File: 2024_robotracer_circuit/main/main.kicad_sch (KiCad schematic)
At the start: 18 parts, among them J1 Conn_01x06, J2 Conn_02x05_Odd_Even, J3 Conn_02x05_Odd_Even, SW1 SW_Push, U1 STM32F405RGTx

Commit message: 進めた
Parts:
- added C11, C14, C15, C18, C20, C21, C23: 0.1u, symbol Device:C_Small
- added C12, C13: 220u, symbol Device:C_Polarized_Small
- added C16, C17, C19, C22: 100u, symbol Device:C_Polarized_Small
- added J4, J5, J6: Conn_01x02, symbol Connector_Generic:Conn_01x02
- added R2: R, symbol Device:R
- added SW2: SW_DPDT_x2, symbol Switch:SW_DPDT_x2
- added U3, U4: ~, symbol mylib:AM2837
- added U5: ~, symbol mylib:BP5293-33
- added U6: ~, symbol mylib:BP5293-50
- added U7: ~, symbol mylib:SSM6J808R
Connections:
- net +3.3V: now also C17.1, C18.1, U5.3 (VOUT)
- net +5V: now also C21.1, C22.1, U6.3 (VOUT)
- net GND: now also C11.2, C12.2, C13.2, C14.2, C15.2, C16.2, C17.2, C18.2, C19.2, C20.2, C21.2, C22.2, C23.2, J6.2 (Pin_2), SW2.2 (B), U3.3 (GND), U4.3 (GND), U5.2 (GND), U6.2 (GND)
- new net: J6.1 (Pin_1), R2.1, U7.4 (SOURCE)
- new net: J4.1 (Pin_1), U3.7 (OUT_A), U3.8 (OUT_A)
- new net: J4.2 (Pin_2), U3.5 (OUT_B), U3.6 (OUT_B)
- new net: R2.2, SW2.1 (A), U7.3 (GATE)
- new net: J5.2 (Pin_2), U4.5 (OUT_B), U4.6 (OUT_B)
- new net: J5.1 (Pin_1), U4.7 (OUT_A), U4.8 (OUT_A)
- new net +BATT: C11.1, C12.1, C13.1, C14.1, C15.1, C16.1, C19.1, C20.1, C23.1, U3.4 (VCC), U4.4 (VCC), U5.1 (VIN), U6.1 (VIN), U7.1 (DRAIN_1), U7.2 (DRAIN_2), U7.5 (DRAIN_3), U7.6 (DRAIN_4)
- new net MOTOR1_IN_A: U3.1 (IN_A), U4.1 (IN_A)
- new net MOTOR1_IN_B: U3.2 (IN_B), U4.2 (IN_B)
- no-connect marks 14 -> 15
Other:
- moved on the sheet: C1, C10, C2, C3, C4, C5, C6, C7, C8, C9, FB1, J1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

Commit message: 途中
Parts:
- added BZ1: Buzzer, symbol Device:Buzzer
- added C24: 220u, symbol Device:C_Polarized_Small
- added C25: 0.1u, symbol Device:C_Small
- added C26, C27: 100u, symbol Device:C_Polarized_Small
- added D1: D, symbol Device:D
- added D2, D3, D4: LED_Small, symbol Device:LED_Small
- added J10, J11: Conn_01x03, symbol Connector_Generic:Conn_01x03
- added J7: Micro_SD_Card_Det1, symbol Connector:Micro_SD_Card_Det1
- added J8: Conn_01x04, symbol Connector_Generic:Conn_01x04
- added J9: Conn_01x06, symbol Connector_Generic:Conn_01x06
- added R11, R12, R13, R14, R15, R16, R17: 22k, symbol Device:R_Small
- added R18, R19, R20, R21, R22, R25, R28: 47k, symbol Device:R_Small
- added R23, R24, R31, R32, R33: R_Small, symbol Device:R_Small
- added R26, R29, R3, R5, R7, R9: 4.7, symbol Device:R_Small
- added R34, R35, R36, R37, R38, R39, R4, R6: 1k, symbol Device:R_Small
- added U10, U12, U14, U17, U18, U20, U9: ~, symbol mylib:MTN2306AN3
- added U11, U13, U15, U19, U21, U8: ~, symbol mylib:LBR-127HLD
- added U16: ~, symbol mylib:AE-BMX055
- J4, J5: value Conn_01x02 -> PA_2p
- J6: value Conn_01x02 -> XT_2p
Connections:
- net +3.3V: now also C24.1, C25.1, J7.4 (VDD), J8.1 (Pin_1), R11.1, R12.1, R13.1, R14.1, R15.1, R16.1, R32.1, R34.1, R35.1, U16.4 (3V3)
- net +5V: now also J10.1 (Pin_1), J11.1 (Pin_1), J9.1 (Pin_1), R33.1, R36.1, R37.1, R38.1, R39.1, R4.1, R6.1, U11.1 (anode), U13.1 (anode), U15.1 (anode), U19.1 (anode), U21.1 (anode), U8.1 (anode)
- net +BATT: now also BZ1.1 (+), C26.1, C27.1, D1.1 (K), R23.1, R31.1
- net GND: now also C24.2, C25.2, C26.2, C27.2, D2.1 (K), D3.1 (K), D4.1 (K), J10.3 (Pin_3), J11.3 (Pin_3), J7.10 (SHIELD), J7.6 (VSS), J8.4 (Pin_4), J9.6 (Pin_6), R17.2, R18.2, R19.2, R20.2, R21.2, R22.2, R24.2, R25.2, R28.2, U10.3 (S), U11.3 (E), U12.3 (S), U13.3 (E), U14.3 (S), U15.3 (E), U16.1 (GND), U17.3 (S), U18.3 (S), U19.3 (E), U20.3 (S), U21.3 (E), U8.3 (E), U9.3 (S)
- new net: R29.1, U21.2 (cathode)
- new net: R29.2, U20.2 (D)
- new net: R26.1, U19.2 (cathode)
- new net: R26.2, U18.2 (D)
- new net: R3.2, U9.2 (D)
- new net: R5.1, U11.2 (cathode)
- new net: D3.2 (A), R32.2
- new net: R3.1, U8.2 (cathode)
- new net: J7.1 (DAT2), R16.2
- new net: R9.1, U15.2 (cathode)
- new net: R9.2, U14.2 (D)
- new net: D4.2 (A), R33.2
- new net: R5.2, U10.2 (D)
- new net: J7.8 (DAT1), R12.2
- new net: D2.2 (A), R31.2
- new net: BZ1.2 (-), D1.2 (A), U17.2 (D)
- new net: J7.2 (DAT3/CD), R15.2
- new net: R7.1, U13.2 (cathode)
- new net: R7.2, U12.2 (D)
- new net BATT_REF: R23.2, R24.1
- new net BZ_PWM: R22.1, U17.1 (G)
- new net IMU_SCL: U16.3 (SCL)
- new net IMU_SDA: U16.2 (SDA)
- new net LCD_SCL: J8.3 (Pin_3), R35.2
- new net LCD_SDA: J8.2 (Pin_2), R34.2
- new net SDIO_CK: J7.5 (CLK), R17.1
- new net SDIO_CMD: J7.3 (CMD), R14.2
- new net SDIO_D0: J7.7 (DAT0), R13.2
- new net SDIO_SW: J7.9 (DET), R11.2
- new net SENSOR0_ADC: J9.2 (Pin_2), R36.2, U8.4 (C)
- new net SENSOR0_PWM: R18.1, U9.1 (G)
- new net SENSOR1_ADC: J9.3 (Pin_3), R37.2, U11.4 (C)
- new net SENSOR1_PWM: R19.1, U10.1 (G)
- new net SENSOR2_ADC: J9.4 (Pin_4), R38.2, U13.4 (C)
- new net SENSOR2_PWM: R20.1, U12.1 (G)
- new net SENSOR3_ADC: J9.5 (Pin_5), R39.2, U15.4 (C)
- new net SENSOR3_PWM: R21.1, U14.1 (G)
- new net SENSOR_L_ADC: J10.2 (Pin_2), R4.2, U19.4 (C)
- new net SENSOR_L_PWM: R25.1, U18.1 (G)
- new net SENSOR_R_ADC: J11.2 (Pin_2), R6.2, U21.4 (C)
- new net SENSOR_R_PWM: R28.1, U20.1 (G)
- no-connect marks 15 -> 17
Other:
- moved on the sheet: C1, C10, C11, C12, C13, C14, C15, C16, C17, C18, C19, C2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

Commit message: ピン割り当て
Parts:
- R1: value R -> 10k
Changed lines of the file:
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@@
 			)
 		)
-		(property "Value" "R"
+		(property "Value" "10k"
 			(at 308.61 74.9299 0)
 			(effects

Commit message: デザインルールOK
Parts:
- added D10, D11, D12, D13, D14, D15, D5, D6, D7, D8, D9: LED_Small, symbol Device:LED_Small
- added FB2: FerriteBead_Small, symbol Device:FerriteBead_Small
- added J12: Conn_01x04, symbol Connector_Generic:Conn_01x04
- added J14: Conn_01x06, symbol Connector_Generic:Conn_01x06
- added R10, R27, R30, R40, R41, R42, R43, R44, R45, R46, R8: R_Small, symbol Device:R_Small
- added U22: ~, symbol mylib:SKRHAAE010
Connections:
- net BATT_REF is gone; now on net BATT_REF_ADC: R23.2, R24.1
- net SWCLC is gone; now on net SWCLK: J1.2 (Pin_2)
- net +3.3V: now also J12.1 (Pin_1), J14.1 (Pin_1)
- net BZ_PWM: now also U1.35 (PB14)
- net ENC1_A: now also U1.58 (PB6)
- net ENC1_B: now also U1.59 (PB7)
- net ENC2_A: now also U1.37 (PC6)
- net ENC2_B: now also U1.38 (PC7)
- net GND: now also D10.1 (K), D11.1 (K), D12.1 (K), D13.1 (K), D14.1 (K), D15.1 (K), D5.1 (K), D6.1 (K), D7.1 (K), D8.1 (K), D9.1 (K), FB2.1, J12.4 (Pin_4), J14.6 (Pin_6), U22.5 (Common)
- net GNDA: now also FB2.2
- net IMU_SCL: now also U1.61 (PB8)
- net IMU_SDA: now also U1.62 (PB9)
- net LCD_SCL: now also U1.29 (PB10)
- net LCD_SDA: now also U1.30 (PB11)
- net MOTOR1_IN_A: now also U1.41 (PA8); no longer U4.1 (IN_A)
- net MOTOR1_IN_B: now also U1.42 (PA9); no longer U4.2 (IN_B)
- net SDIO_CK: now also U1.53 (PC12)
- net SDIO_CMD: now also U1.54 (PD2)
- net SDIO_D0: now also U1.39 (PC8)
- net SDIO_SW: now also U1.50 (PA15)
- net SENSOR0_ADC: now also U1.14 (PA0)
- net SENSOR1_ADC: now also U1.15 (PA1)
- net SENSOR2_ADC: now also U1.16 (PA2)
- net SENSOR3_ADC: now also U1.17 (PA3)
- net SENSOR_L_ADC: now also U1.20 (PA4)
- net SENSOR_R_ADC: now also U1.21 (PA5)
- net SWDIO: now also U1.46 (PA13)
- net SWO: now also U1.55 (PB3)
- net SPI_MISO_GP: now reaches U1.10 (PC2)
- net SPI_MISO_GP: now also J14.2 (Pin_2)
- net SPI_MOSI_GP: now reaches U1.11 (PC3)
- net SPI_MOSI_GP: now also J14.3 (Pin_3)
- net LED3: now reaches U1.2 (PC13)
- net LED3: now also R30.1
- net BATT_REF_ADC: now reaches U1.22 (PA6)
- net SW_A: now reaches U1.23 (PA7)
- net SW_A: now also U22.1 (A)
- net SW_B: now reaches U1.24 (PC4)
- net SW_B: now also U22.4 (B)
- net SW_Center: now reaches U1.25 (PC5)
- net SW_Center: now also U22.2 (Center)
- net SW_C: now reaches U1.26 (PB0)
- net SW_C: now also U22.3 (C)
- net SW_D: now reaches U1.27 (PB1)
- net SW_D: now also U22.6 (D)
- net LED9: now reaches U1.28 (PB2)
- net LED9: now also R45.1
- net LED4: now reaches U1.3 (PC14)
- net LED4: now also R40.1
- net LED6: now reaches U1.33 (PB12)
- net LED6: now also R42.1
- net SPI_SCK_GP: now reaches U1.34 (PB13)
- net SPI_SCK_GP: now also J14.4 (Pin_4)
- net PWM_GP: now reaches U1.36 (PB15)
- net PWM_GP: now also J14.5 (Pin_5)
- net LED5: now reaches U1.4 (PC15)
- net LED5: now also R41.1
- net LED2: now reaches U1.40 (PC9)
- net LED2: now also R27.1
- net MOTOR2_IN_A: now reaches U1.43 (PA10)
- net MOTOR2_IN_A: now also U4.1 (IN_A)
- net MOTOR2_IN_B: now reaches U1.44 (PA11)
- net MOTOR2_IN_B: now also U4.2 (IN_B)
- net LED10: now reaches U1.45 (PA12)
- net LED10: now also R46.1
- net SWCLK: now reaches U1.49 (PA14)
- net USART_TX: now reaches U1.51 (PC10)
- net USART_TX: now also J12.2 (Pin_2)
- net USART_RX: now reaches U1.52 (PC11)
- net USART_RX: now also J12.3 (Pin_3)
- net LED8: now reaches U1.56 (PB4)
- net LED8: now also R44.1
- net LED7: now reaches U1.57 (PB5)
- net LED7: now also R43.1
- net LED0: now reaches U1.8 (PC0)
- net LED0: now also R8.1
- net LED1: now reaches U1.9 (PC1)
- net LED1: now also R10.1
- new net: D10.2 (A), R41.2
- new net: D9.2 (A), R40.2
- new net: D11.2 (A), R42.2
- new net: D12.2 (A), R43.2
- new net: D14.2 (A), R45.2
- new net: D8.2 (A), R30.2
- new net: D7.2 (A), R27.2
- new net: D5.2 (A), R8.2
- new net: D15.2 (A), R46.2
- new net: D6.2 (A), R10.2
- new net: D13.2 (A), R44.2
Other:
- moved on the sheet: BZ1, C24, C25, C3, C4, D1, FB1, J1, J10, J11, J7, J8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

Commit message: フットプリント割り当て中
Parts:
- removed C26, C27: 100u, symbol Device:C_Polarized_Small
- removed SW2: SW_DPDT_x2, symbol Switch:SW_DPDT_x2
- added U23: ~, symbol mylib:Toggle_SW
- C1, C10, C11, C14, C15, C18, C2, C20, C21, C23, C25, C3, C4, C5, C6, C7, C8, C9: footprint (none) -> Capacitor_SMD:C_0603_1608Metric_Pad1.08x0.95mm_HandSolder
- C12, C13, C24: value 220u -> 100u; footprint (none) -> Capacitor_SMD:CP_Elec_6.3x5.4
- C16, C17, C19, C22: footprint (none) -> Capacitor_SMD:CP_Elec_6.3x5.4
- D1: value D -> BAT54ST; footprint (none) -> Package_TO_SOT_SMD:SOT-523
- D10, D11, D12, D13, D14, D15, D2, D3, D4, D5, D6, D7, D8, D9: footprint (none) -> LED_SMD:LED_0603_1608Metric_Pad1.05x0.95mm_HandSolder
- FB1, FB2, J7, R1, R10, R11, R12, R13, R14, R15, R16, R17, R18, R19, R2, R20, R21, R22, R23, R24, R25, R26, R27, R28, R29, R3, R30, R31, R32, R33, R34, R35, R36, R37, R38, R39, R4, R40, R41, R42, R43, R44, R45, R46, R5, R6, R7, R8, R9: footprint (none) -> Resistor_SMD:R_0603_1608Metric_Pad0.98x0.95mm_HandSolder
- J1: value Conn_01x06 -> PH_6p; footprint (none) -> Connector_JST:JST_PH_B6B-PH-K_1x06_P2.00mm_Vertical
- J10, J11: value Conn_01x03 -> PH_3p; footprint (none) -> Resistor_SMD:R_0603_1608Metric_Pad0.98x0.95mm_HandSolder
- J12, J8: value Conn_01x04 -> PH_4p; footprint (none) -> Resistor_SMD:R_0603_1608Metric_Pad0.98x0.95mm_HandSolder
- J14, J9: value Conn_01x06 -> PH_6p; footprint (none) -> Resistor_SMD:R_0603_1608Metric_Pad0.98x0.95mm_HandSolder
- J2, J3: footprint (none) -> Connector_PinHeader_1.00mm:PinHeader_2x05_P1.00mm_Vertical
- J4, J5: footprint (none) -> Connector_JST:JST_PH_B2B-PH-K_1x02_P2.00mm_Vertical
- J6: footprint (none) -> Connector_AMASS:AMASS_XT30U-M_1x02_P5.0mm_Vertical
- U21: value ~ -> LBR-127HLD
- U22: value ~ -> SKRHAAE010
- U3, U4: value ~ -> AM2837; footprint (none) -> Package_SO:TSSOP-8_3x3mm_P0.65mm
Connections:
- net GND: now also U23.2
- net at R2.2, U7.3 (GATE): now also U23.1
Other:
- moved on the sheet: J9, R36, R37, R38, R39

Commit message: とちゅう
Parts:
- U10, U12, U14, U17, U18, U20, U9: value ~ -> MTN2306AN3
- U11, U13, U15, U19, U8: value ~ -> LBR-127HLD
- U16: value ~ -> AE-BMX055
- U2: value ~ -> OSC8MI/H
- U5: value ~ -> BP5293-33
- U6: value ~ -> BP5293-50
- U7: value ~ -> SSM6J808R
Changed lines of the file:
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@@
 		(dnp no)
 		(property "Reference" "U2"
-			(at 318.262 71.882 0)
+			(at 318.516 70.104 0)
 			(effects
 				(font
@@
 			)
 		)
-		(property "Value" "~"
+		(property "Value" "OSC8MI/H"
 			(at 318.135 72.39 0)
 			(effects
@@
 			)
 		)
-		(property "Value" "~"
+		(property "Value" "MTN2306AN3"
 			(at 173.99 158.75 90)
 			(effects
@@
 			)
 		)
-		(property "Value" "~"
+		(property "Value" "MTN2306AN3"
 			(at 172.72 222.25 90)
 			(effects
@@
 			)
 		)
-		(property "Value" "~"
+		(property "Value" "AE-BMX055"
 			(at 345.44 180.34 0)
 			(effects
@@
 			)
 		)
-		(property "Value" "~"
+		(property "Value" "LBR-127HLD"
 			(at 229.87 195.58 0)
 			(effects
@@
 	)
 	(symbol
+		(lib_name "LBR-127HLD_5")
 		(lib_id "mylib:LBR-127HLD")
 		(at 185.42 201.93 0)
@@
 			)
 		)
-		(property "Value" "~"
+		(property "Value" "LBR-127HLD"
 			(at 185.42 195.58 0)
 			(effects
@@
 			)
 		)
-		(property "Value" "~"
+		(property "Value" "MTN2306AN3"
 			(at 309.88 222.25 90)
 			(effects
@@
 	)
 	(symbol
+		(lib_name "MTN2306AN3_3")
 		(lib_id "mylib:MTN2306AN3")
 		(at 220.98 157.48 90)
@@
 			)
 		)
-		(property "Value" "~"
+		(property "Value" "MTN2306AN3"
 			(at 218.44 158.75 90)
 			(effects
@@
 			)
 		)
-		(property "Value" "~"
+		(property "Value" "SSM6J808R"
 			(at 52.07 29.21 0)
 			(effects
@@
 			)
 		)
-		(property "Value" "~"
+		(property "Value" "MTN2306AN3"
 			(at 217.17 222.25 90)
 			(effects
@@
 			)
 		)
-		(property "Value" "~"
+		(property "Value" "MTN2306AN3"
 			(at 34.29 91.44 90)
 			(effects
@@
 			)
 		)
-		(property "Value" "~"
+		(property "Value" "LBR-127HLD"
 			(at 186.69 132.08 0)
 			(effects
@@
 			)
 		)
-		(property "Value" "~"
+		(property "Value" "BP5293-33"
 			(at 139.7 34.29 0)
 			(effects
@@
 			)
 		)
-		(property "Value" "~"
+		(property "Value" "LBR-127HLD"
 			(at 322.58 195.58 0)
 			(effects
@@
 			)
 		)
-		(property "Value" "~"
+		(property "Value" "MTN2306AN3"
 			(at 264.16 222.25 90)
 			(effects
@@
 	)
 	(symbol
-		(lib_name "LBR-127HLD_1")
 		(lib_id "mylib:LBR-127HLD")
 		(at 231.14 138.43 0)
@@
 			)
 		)
-		(property "Value" "~"
+		(property "Value" "LBR-127HLD"
 			(at 276.86 195.58 0)
 			(effects
@@
 			)
 		)
-		(property "Value" "~"
+		(property "Value" "BP5293-50"
 			(at 229.87 35.56 0)
 			(effects

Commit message: フットプリント割り当て中
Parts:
- U10, U12, U14, U17, U18, U20, U9: footprint (none) -> Package_TO_SOT_SMD:SOT-23
- U16: footprint (none) -> mylib:AE-BMX055
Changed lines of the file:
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@@
 			)
 		)
-		(property "Footprint" ""
+		(property "Footprint" "Package_TO_SOT_SMD:SOT-23"
 			(at 176.53 157.48 0)
 			(effects
@@
 			)
 		)
-		(property "Footprint" ""
+		(property "Footprint" "Package_TO_SOT_SMD:SOT-23"
 			(at 175.26 220.98 0)
 			(effects
@@
 			)
 		)
-		(property "Footprint" ""
+		(property "Footprint" "mylib:AE-BMX055"
 			(at 345.44 177.8 0)
 			(effects
@@
 			)
 		)
-		(property "Footprint" ""
+		(property "Footprint" "Package_TO_SOT_SMD:SOT-23"
 			(at 312.42 220.98 0)
 			(effects
@@
 			)
 		)
-		(property "Footprint" ""
+		(property "Footprint" "Package_TO_SOT_SMD:SOT-23"
 			(at 220.98 157.48 0)
 			(effects
@@
 			)
 		)
-		(property "Footprint" ""
+		(property "Footprint" "Package_TO_SOT_SMD:SOT-23"
 			(at 219.71 220.98 0)
 			(effects
@@
 			)
 		)
-		(property "Footprint" ""
+		(property "Footprint" "Package_TO_SOT_SMD:SOT-23"
 			(at 36.83 90.17 0)
 			(effects
@@
 			)
 		)
-		(property "Footprint" ""
+		(property "Footprint" "Package_TO_SOT_SMD:SOT-23"
 			(at 266.7 220.98 0)
 			(effects

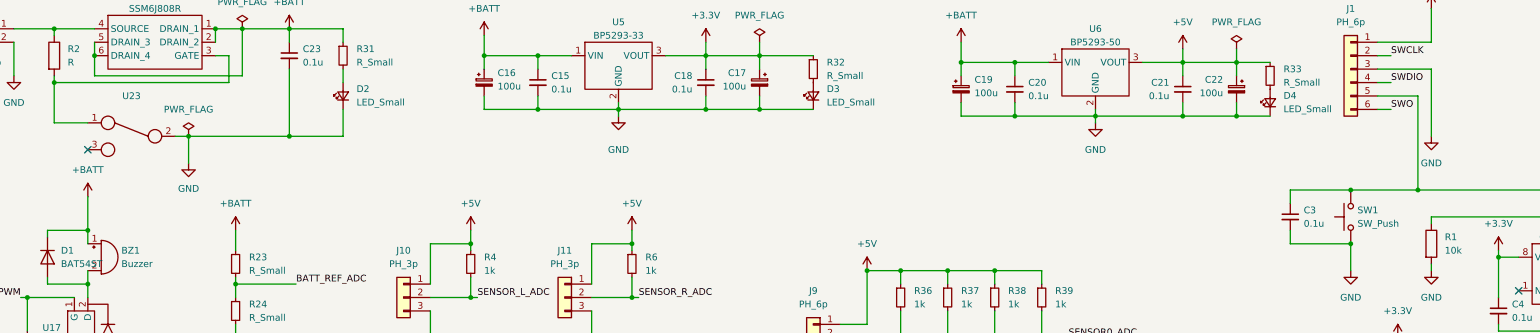
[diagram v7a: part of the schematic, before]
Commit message: フットプリント割り当ておわり
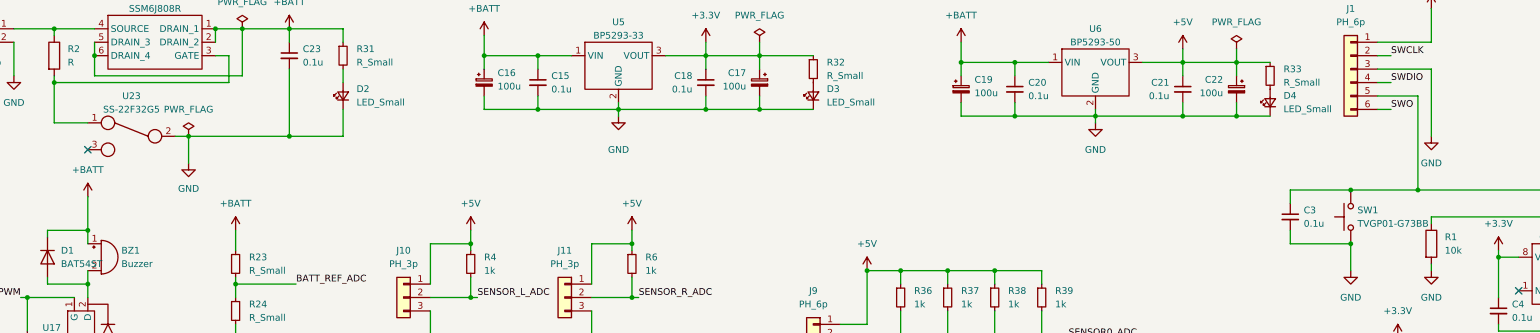
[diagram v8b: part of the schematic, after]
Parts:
- BZ1: footprint (none) -> mylib:UM1515IA085008
- J10, J11: footprint Resistor_SMD:R_0603_1608Metric_Pad0.98x0.95mm_HandSolder -> Connector_JST:JST_PH_B3B-PH-K_1x03_P2.00mm_Vertical
- J12, J8: footprint Resistor_SMD:R_0603_1608Metric_Pad0.98x0.95mm_HandSolder -> Connector_JST:JST_PH_B4B-PH-K_1x04_P2.00mm_Vertical
- J14, J9: footprint Resistor_SMD:R_0603_1608Metric_Pad0.98x0.95mm_HandSolder -> Connector_JST:JST_PH_B6B-PH-K_1x06_P2.00mm_Vertical
- J7: footprint Resistor_SMD:R_0603_1608Metric_Pad0.98x0.95mm_HandSolder -> Connector_Card:microSD_HC_Hirose_DM3AT-SF-PEJM5
- SW1: value SW_Push -> TVGP01-G73BB; footprint (none) -> mylib:TVGP01-G73BB
- U11, U13, U15, U19, U21, U8: footprint (none) -> mylib:LBR-127HLD
- U2: footprint (none) -> mylib:OSC8MIH
- U22: footprint (none) -> mylib:SKRHAAE010
- U23: value ~ -> SS-22F32G5; footprint (none) -> Connector_PinHeader_2.54mm:PinHeader_1x03_P2.54mm_Vertical
- U5, U6: footprint (none) -> mylib:BP5293-xx
- U7: footprint (none) -> Package_SO:TSOP-6_1.65x3.05mm_P0.95mm
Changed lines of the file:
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@@
 			)
 		)
-		(property "Footprint" ""
+		(property "Footprint" "mylib:OSC8MIH"
 			(at 316.23 78.74 0)
 			(effects
@@
 			)
 		)
-		(property "Footprint" "Resistor_SMD:R_0603_1608Metric_Pad0.98x0.95mm_HandSolder"
+		(property "Footprint" "Connector_JST:JST_PH_B6B-PH-K_1x06_P2.00mm_Vertical"
 			(at 176.53 93.98 0)
 			(effects
@@
 			)
 		)
-		(property "Footprint" "Resistor_SMD:R_0603_1608Metric_Pad0.98x0.95mm_HandSolder"
+		(property "Footprint" "Connector_JST:JST_PH_B4B-PH-K_1x04_P2.00mm_Vertical"
 			(at 279.4 134.62 0)
 			(effects
@@
 			)
 		)
-		(property "Footprint" "Resistor_SMD:R_0603_1608Metric_Pad0.98x0.95mm_HandSolder"
+		(property "Footprint" "Connector_JST:JST_PH_B4B-PH-K_1x04_P2.00mm_Vertical"
 			(at 279.4 104.14 0)
 			(effects
@@
 			)
 		)
-		(property "Footprint" "Resistor_SMD:R_0603_1608Metric_Pad0.98x0.95mm_HandSolder"
+		(property "Footprint" "Connector_JST:JST_PH_B6B-PH-K_1x06_P2.00mm_Vertical"
 			(at 279.4 166.37 0)
 			(effects
@@
 			)
 		)
-		(property "Footprint" ""
+		(property "Footprint" "mylib:LBR-127HLD"
 			(at 228.6 201.93 0)
 			(effects
@@
 			)
 		)
-		(property "Footprint" ""
+		(property "Footprint" "mylib:LBR-127HLD"
 			(at 184.15 201.93 0)
 			(effects
@@
 			)
 		)
-		(property "Value" "SW_Push"
+		(property "Value" "TVGP01-G73BB"
 			(at 279.4 69.8499 90)
 			(effects
@@
 			)
 		)
-		(property "Footprint" ""
+		(property "Footprint" "mylib:TVGP01-G73BB"
 			(at 273.05 68.58 0)
 			(effects
@@
 			)
 		)
-		(property "Footprint" ""
+		(property "Footprint" "mylib:SKRHAAE010"
 			(at 142.24 181.61 0)
 			(effects
@@
 			)
 		)
-		(property "Footprint" ""
+		(property "Footprint" "Package_SO:TSOP-6_1.65x3.05mm_P0.95mm"
 			(at 52.07 34.29 0)
 			(effects
@@
 			)
 		)
-		(property "Footprint" ""
+		(property "Footprint" "mylib:LBR-127HLD"
 			(at 185.42 138.43 0)
 			(effects
@@
 			)
 		)
-		(property "Footprint" "Resistor_SMD:R_0603_1608Metric_Pad0.98x0.95mm_HandSolder"
+		(property "Footprint" "Connector_Card:microSD_HC_Hirose_DM3AT-SF-PEJM5"
 			(at 172.72 120.65 0)
 			(effects
@@
 			)
 		)
-		(property "Footprint" ""
+		(property "Footprint" "mylib:BP5293-xx"
 			(at 139.7 38.1 0)
 			(effects
@@
 			)
 		)
-		(property "Footprint" ""
+		(property "Footprint" "mylib:LBR-127HLD"
 			(at 321.31 201.93 0)
 			(effects
@@
 			)
 		)
-		(property "Value" "~"
+		(property "Value" "SS-22F32G5"
 			(at 47.625 48.26 0)
 			(effects
@@
 			)
 		)
-		(property "Footprint" ""
+		(property "Footprint" "Connector_PinHeader_2.54mm:PinHeader_1x03_P2.54mm_Vertical"
 			(at 46.99 53.34 0)
 			(effects
@@
 			)
 		)
-		(property "Footprint" "Resistor_SMD:R_0603_1608Metric_Pad0.98x0.95mm_HandSolder"
+		(property "Footprint" "Connector_JST:JST_PH_B3B-PH-K_1x03_P2.00mm_Vertical"
 			(at 99.06 83.82 0)
 			(effects
@@
 			)
 		)
-		(property "Footprint" "Resistor_SMD:R_0603_1608Metric_Pad0.98x0.95mm_HandSolder"
+		(property "Footprint" "Connector_JST:JST_PH_B3B-PH-K_1x03_P2.00mm_Vertical"
 			(at 129.54 83.82 0)
 			(effects
@@
 			)
 		)
-		(property "Footprint" ""
+		(property "Footprint" "mylib:UM1515IA085008"
 			(at 41.275 73.66 90)
 			(effects
@@
 			)
 		)
-		(property "Footprint" ""
+		(property "Footprint" "mylib:LBR-127HLD"
 			(at 229.87 138.43 0)
 			(effects
@@
 			)
 		)
-		(property "Footprint" ""
+		(property "Footprint" "mylib:LBR-127HLD"
 			(at 275.59 201.93 0)
 			(effects
@@
 			)
 		)
-		(property "Footprint" ""
+		(property "Footprint" "mylib:BP5293-xx"
 			(at 229.87 39.37 0)
 			(effects
